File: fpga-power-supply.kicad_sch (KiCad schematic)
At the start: 88 parts

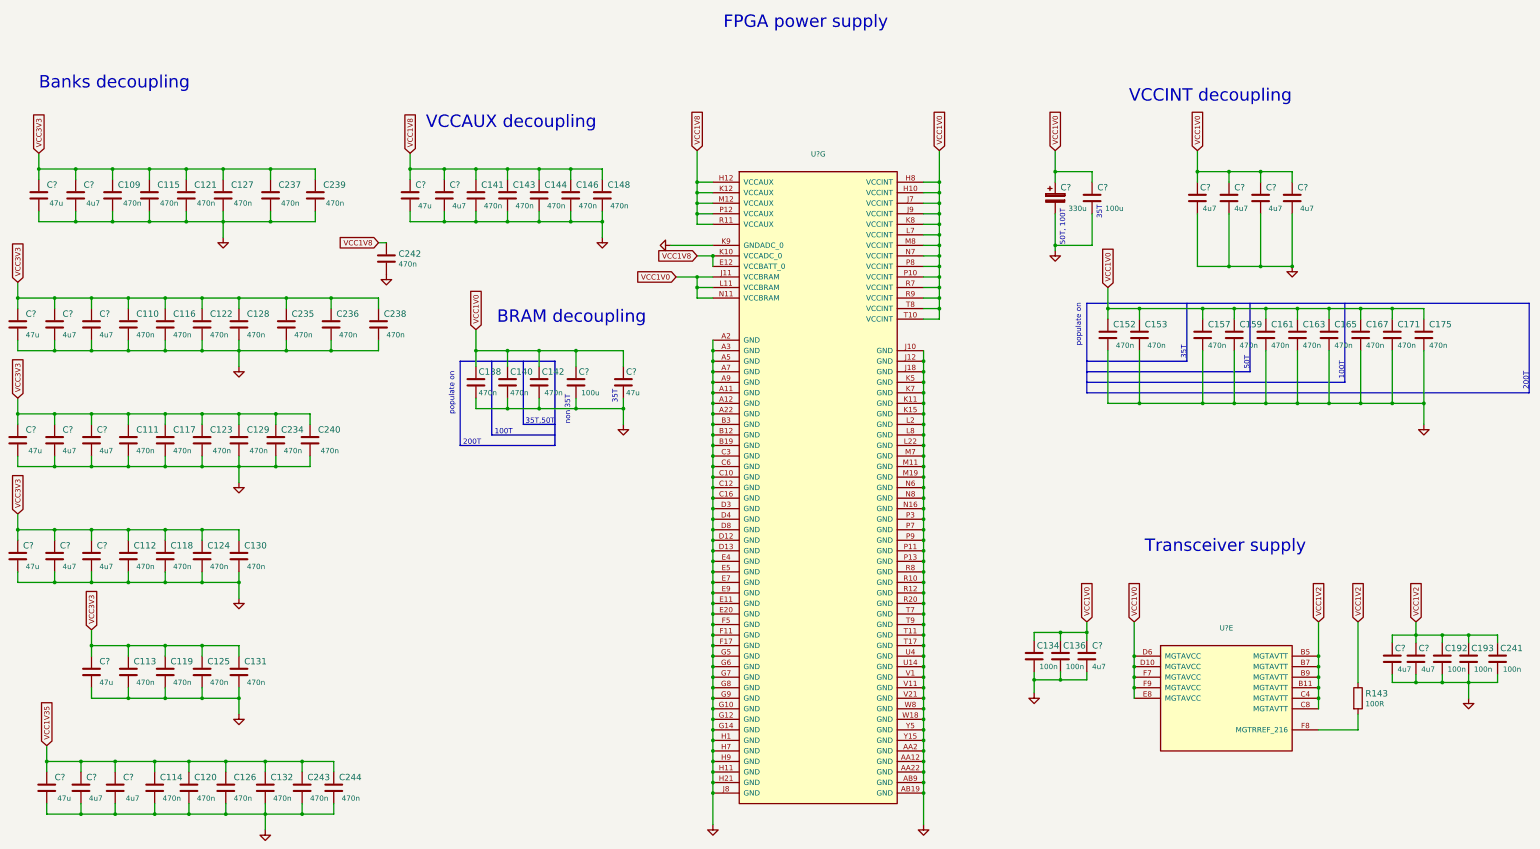
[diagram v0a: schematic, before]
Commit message: Introduce component standardization
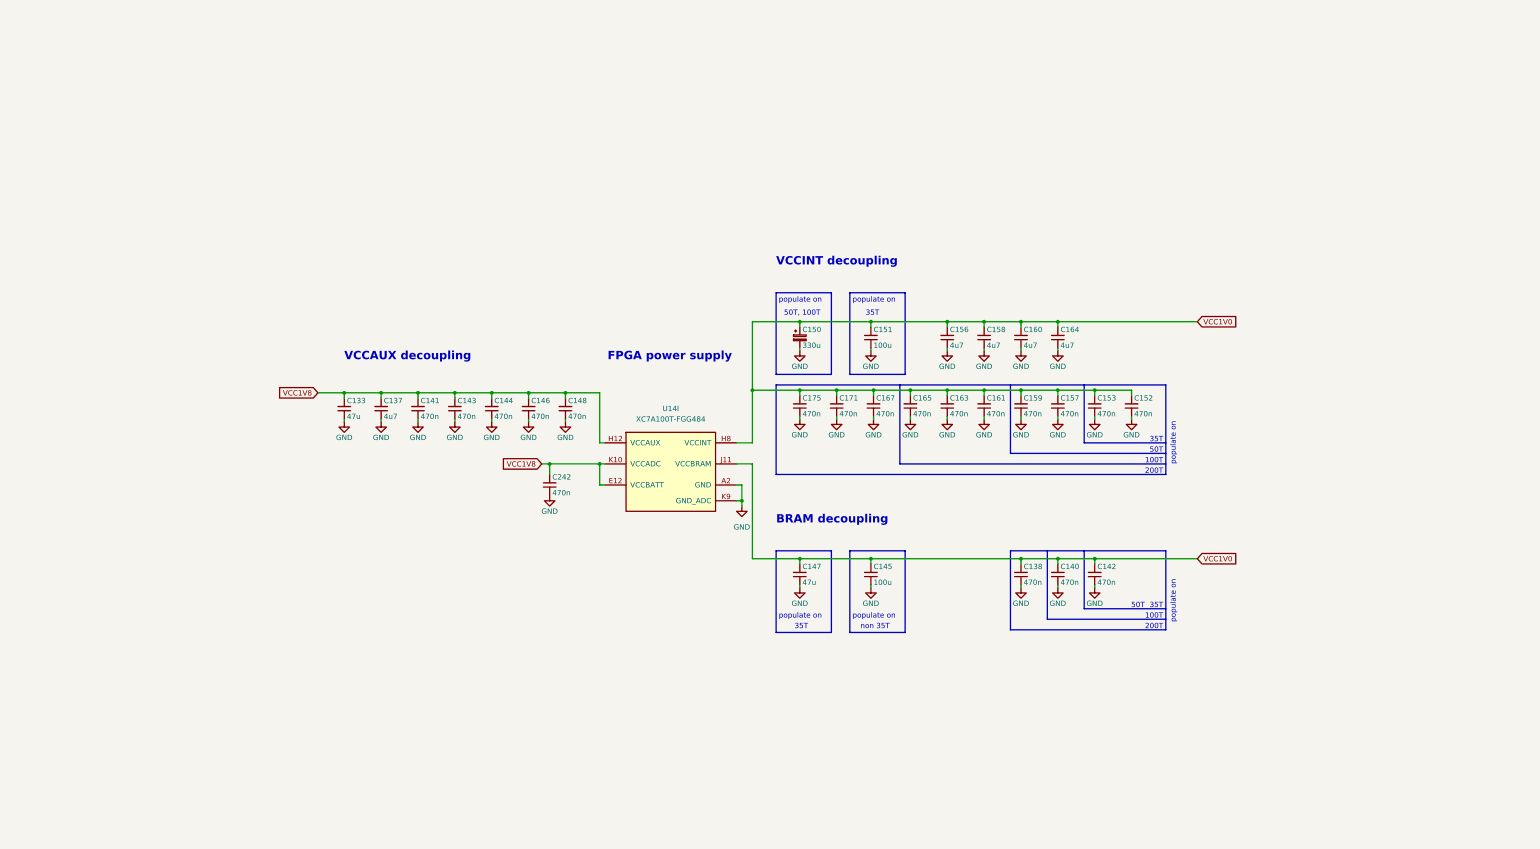
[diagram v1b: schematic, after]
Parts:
- removed C109, C110, C111, C112, C113, C114, C115, C116, C117, C118, C119, C120, C121, C122, C123, C124, C125, C126, C127, C128, C129, C130, C131, C132, C234, C235, C236, C237, C238, C239, C240, C243, C244: (no value), symbol artix-dc-scm:C_470n_0402
- removed C134, C136, C192, C193, C241: (no value), symbol artix-dc-scm:C_100n_0402-artix-dc-scm
- removed C? (x12): (no value), symbol artix-dc-scm:C_4u7_0603
- removed C? (x6): (no value), symbol artix-dc-scm:C_47u_1210
- removed R143: (no value), symbol artix-dc-scm:R_100R_0402
- removed U?: (no value), symbol artix-dc-scm:XC7A100T-FGG484
- C133, C147: renamed from C?; value (none) -> C_47u_1210; footprint (none) -> antmicro-footprints:C_1210_3225Metric; symbol artix-dc-scm:C_47u_1210 -> antmicroCapacitorsmisc:C_47u_1210; Author (none) -> Antmicro; License (none) -> Apache-2.0
- C137, C156, C158, C160, C164: renamed from C?; value (none) -> C_4u7_0603; footprint (none) -> antmicro-footprints:C_0603_1608Metric; symbol artix-dc-scm:C_4u7_0603 -> antmicroCapacitors0603:C_4u7_0603; Author (none) -> Antmicro; License (none) -> Apache-2.0; MPN 0603X475K250CT -> C1608X5R1V475M080AC; Manufacturer WALSIN -> TDK
- C138, C142, C146, C152, C153, C157, C159, C161, C163, C165, C171, C175, C242: value (none) -> C_470n_0201; footprint (none) -> antmicro-footprints:C_0201; symbol artix-dc-scm:C_470n_0201 -> antmicroCapacitorsmisc:C_470n_0201; Author (none) -> Antmicro; License (none) -> Apache-2.0
- C140, C141, C143, C144, C148, C167: value (none) -> C_470n_0402; footprint (none) -> antmicro-footprints:C_0402_1005Metric; symbol artix-dc-scm:C_470n_0402 -> antmicroCapacitors0402:C_470n_0402; Author (none) -> Antmicro; License (none) -> Apache-2.0
- C145, C151: renamed from C?; value (none) -> C_100u_1210; footprint (none) -> antmicro-footprints:C_1210_3225Metric; symbol artix-dc-scm:C_100u_1210 -> antmicroCapacitorsmisc:C_100u_1210; Author (none) -> Antmicro; License (none) -> Apache-2.0; Manufacturer SAMSUNG -> Samsung
- C150: renamed from C?; value (none) -> C_330u_KEMET_D; footprint (none) -> antmicro-footprints:KEMET_D; symbol artix-dc-scm:C_330u_KEMET_D -> antmicroCapacitorspol:C_330u_KEMET_D; Author (none) -> Antmicro; License (none) -> Apache-2.0
- U14: renamed from U?; value (none) -> XC7A100T-FGG484; footprint (none) -> antmicro-footprints:BGA-484_23x23mm_Layout22x22_P1mm_Xilinx_FGG484; symbol artix-dc-scm:XC7A100T-FGG484 -> antmicroMicrocontrollers:XC7A100T-FGG484; Author (none) -> Antmicro; License (none) -> Apache-2.0; MPN (none) -> XC7A100T-FGG484; Manufacturer (none) -> Xilinx
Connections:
- net GND: now also C133.1, C137.1, C138.1, C140.1, C141.1, C142.1, C143.1, C144.1, C145.1, C146.1, C147.1, C148.1, C151.1, C152.1, C153.1, C156.1, C157.1, C158.1, C159.1, C160.1, C161.1, C163.1, C164.1, C165.1, C167.1, C171.1, C175.1, C242.1; no longer C133.2, C137.2, C138.2, C140.2, C141.2, C142.2, C143.2, C144.2, C145.2, C146.2, C147.2, C148.2, C151.2, C152.2, C153.2, C156.2, C157.2, C158.2, C159.2, C160.2, C161.2, C163.2, C164.2, C165.2, C167.2, C171.2, C175.2, C242.2
- net VCC1V0: now also C138.2, C140.2, C142.2, C145.2, C147.2, C151.2, C152.2, C153.2, C156.2, C157.2, C158.2, C159.2, C160.2, C161.2, C163.2, C164.2, C165.2, C167.2, C171.2, C175.2; no longer C138.1, C140.1, C142.1, C145.1, C147.1, C151.1, C152.1, C153.1, C156.1, C157.1, C158.1, C159.1, C160.1, C161.1, C163.1, C164.1, C165.1, C167.1, C171.1, C175.1
- net VCC1V8: now also C133.2, C137.2, C141.2, C143.2, C144.2, C146.2, C148.2, C242.2; no longer C133.1, C137.1, C141.1, C143.1, C144.1, C146.1, C148.1, C242.1
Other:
- note removed: "35T,50T"
- note removed: "Banks decoupling"
- note removed: "Transceiver supply"
- moved on the sheet: C133, C137, C138, C140, C141, C142, C143, C144, C145, C146, C147, C148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
